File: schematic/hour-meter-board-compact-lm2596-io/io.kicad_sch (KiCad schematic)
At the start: 15 parts, among them J902 5V AIN1 GND DOUT1 GND, U901 ADS1115IDGST, U902 SN74AHCT1G125DBVR, U903 BSP75N

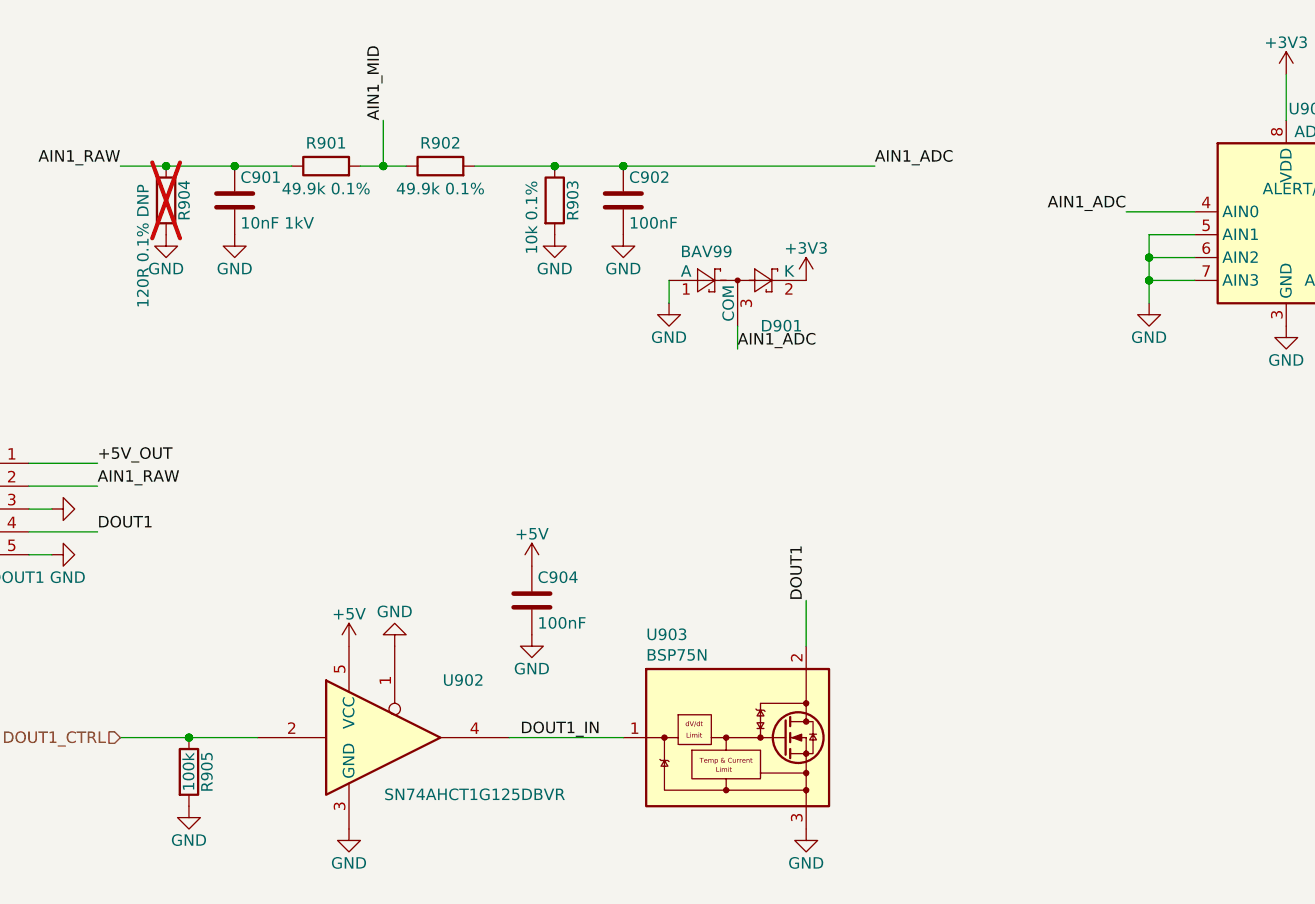
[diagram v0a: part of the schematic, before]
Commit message: fix(pcb): link the I/O board's TP101/TP102 solder pads to their nets
- TP101 (VIN) and TP102 (GND) replace the two-hole TP101: 1.5 mm pads on
  the back, above and below J101. They were placed by hand in the PCB
  editor, so they had no symbol link and no net and could not be routed
- they are now library footprints flipped to the bottom and linked to
  their symbols. A 0.5 mm B.Cu track joins J101 pin 1 to TP101, and TP102
  joins the GND pour solid (its thermal spokes were thinner than the
  pour's minimum)
- pours refilled, so the clearance and solder-mask errors are gone:
  DRC 0 errors, 0 unconnected, 0 parity
- tools-pcb.py: TP101/TP102 placed on the bottom side; `reuse` leaves out
  the LM2596 board's route to its two-hole TP101, which would cross TP102
- includes the board move and the KiCad 10 re-save of the sheets
- production: Gerbers and CPL regenerated, BOM unchanged
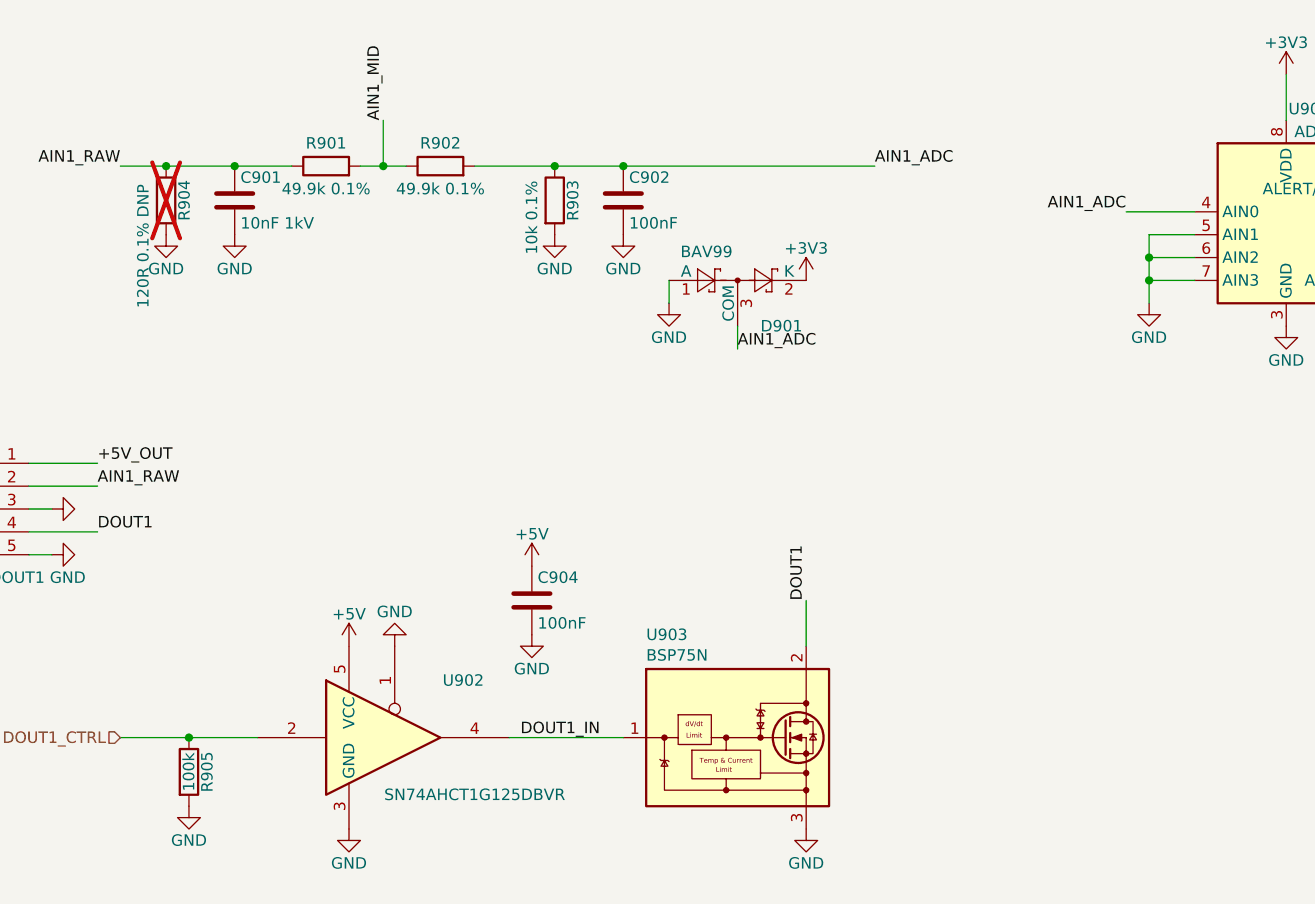
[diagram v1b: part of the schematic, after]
